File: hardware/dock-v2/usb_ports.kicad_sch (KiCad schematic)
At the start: 33 parts, among them J201 TYPE-C-31-M-12, J202 TYPE-C-31-M-12, J203 TYPE-C-31-M-12, U201 TPD4E1U06DBVR, U202 SY6280AAC, U203 TPD4E1U06DBVR, U204 TPD4E1U06DBVR

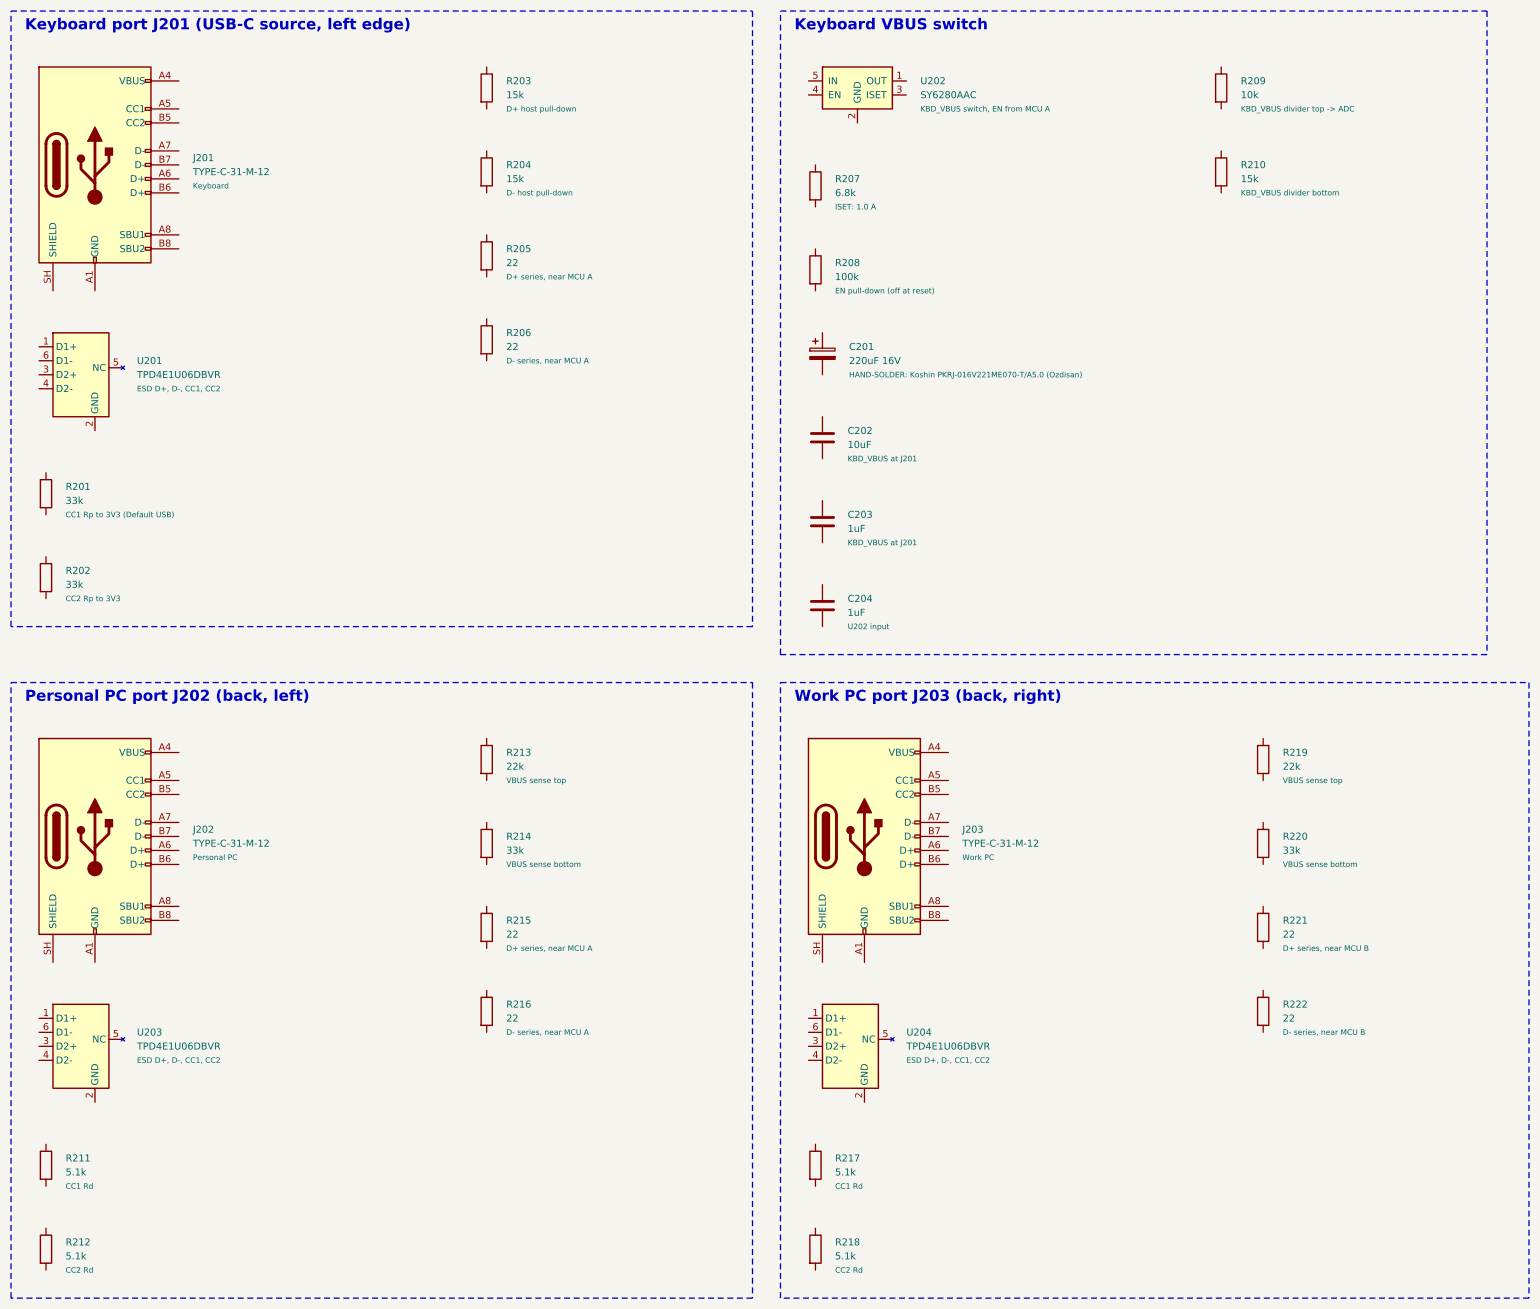
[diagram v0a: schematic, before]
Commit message: Dock v2 schematic: wiring in progress (user's work, snapshot before fixes)
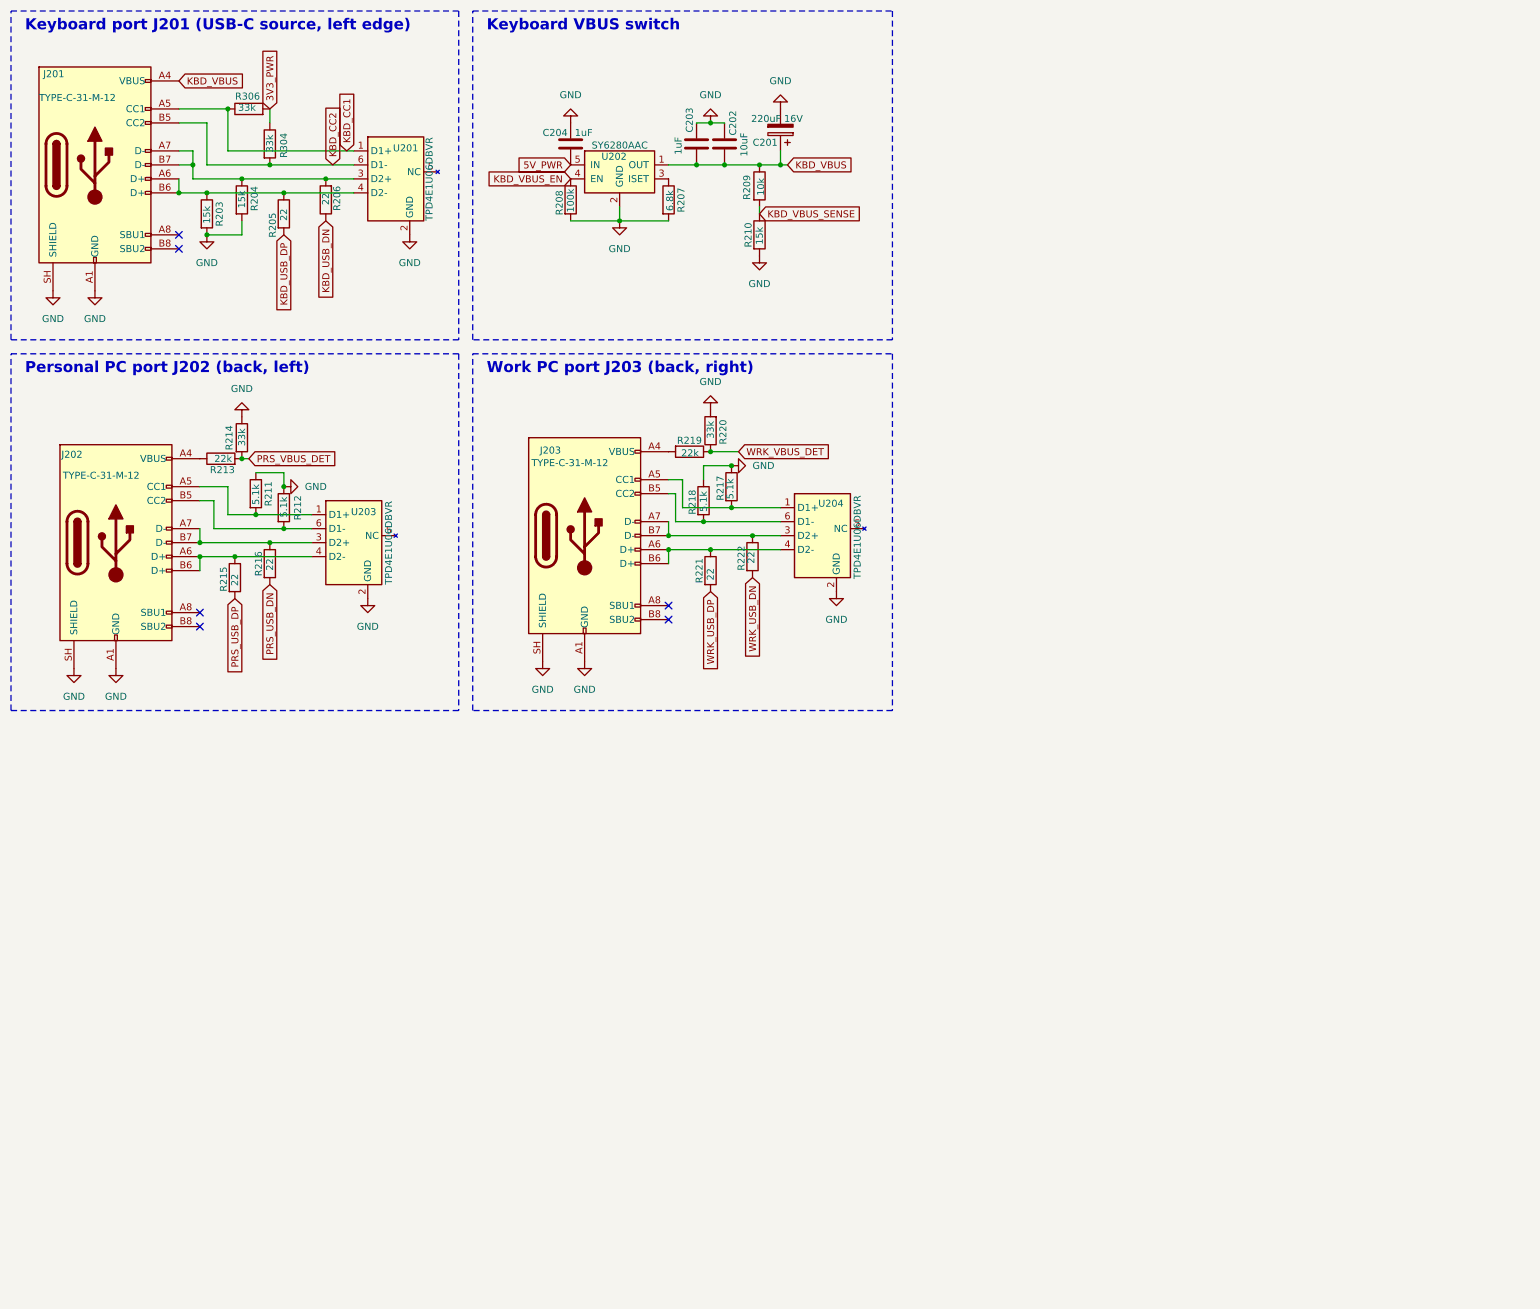
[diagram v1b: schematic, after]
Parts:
- removed R201, R202: 33k, Resistor_SMD:R_0402_1005Metric, symbol Device:R
- added R304, R306: 33k, Resistor_SMD:R_0402_1005Metric, symbol Device:R
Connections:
- net WRK_VBUS_DET: now reaches R219.1
- net WRK_VBUS_DET: now also R220.1
- net at R219.2: now also J203.A4 (VBUS), J203.A9 (VBUS), J203.B4 (VBUS), J203.B9 (VBUS)
- net GND: now reaches R217.1
- net GND: now also C201.2, C202.1, C203.2, C204.1, J201.A1 (GND), J201.A12 (GND), J201.B1 (GND), J201.B12 (GND), J201.SH (SHIELD), J202.A1 (GND), J202.A12 (GND), J202.B1 (GND), J202.B12 (GND), J202.SH (SHIELD), J203.A1 (GND), J203.A12 (GND), J203.B1 (GND), J203.B12 (GND), J203.SH (SHIELD), R203.2, R204.2, R207.2, R208.2, R210.2, R211.1, R212.1, R214.1, R218.1, R220.2, U201.2 (GND), U202.2 (GND), U203.2 (GND), U204.2 (GND)
- net at R217.2: now also J203.A5 (CC1), U204.1 (D1+)
- net PRS_VBUS_DET: now reaches R214.2
- net PRS_VBUS_DET: now also R213.2
- net KBD_VBUS: now reaches C201.1
- net KBD_VBUS: now also C202.2, C203.1, J201.A4 (VBUS), J201.A9 (VBUS), J201.B4 (VBUS), J201.B9 (VBUS), R209.1, U202.1 (OUT)
- net at U203.1 (D1+): now also J202.A5 (CC1), R211.2
- net at U203.3 (D2+): now also J202.A7 (D-), J202.B7 (D-), R216.1
- net at U203.4 (D2-): now also J202.A6 (D+), J202.B6 (D+), R215.1
- net at U203.6 (D1-): now also J202.B5 (CC2), R212.2
- net KBD_VBUS_EN: now reaches R208.1
- net KBD_VBUS_EN: now also U202.4 (EN)
- net KBD_VBUS_SENSE: now reaches R209.2
- net KBD_VBUS_SENSE: now also R210.1
- net KBD_CC1: now reaches J201.A5 (CC1)
- net KBD_CC1: now also U201.1 (D1+), R306.1
- net at J201.A6 (D+): now also J201.B6 (D+), R203.1, R205.1, U201.4 (D2-)
- net at J201.A7 (D-): now also J201.B7 (D-), R204.1, R206.2, U201.3 (D2+)
- net KBD_CC2: now reaches J201.B5 (CC2)
- net KBD_CC2: now also U201.6 (D1-), R304.2
- net at R207.1: now also U202.3 (ISET)
- net at J202.A4 (VBUS), J202.A9 (VBUS), J202.B4 (VBUS)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: now also R213.1
- net at U204.3 (D2+): now also J203.A7 (D-), J203.B7 (D-), R222.1
- net at U204.4 (D2-): now also J203.A6 (D+), J203.B6 (D+), R221.1
- net at U204.6 (D1-): now also J203.B5 (CC2), R218.2
- net PRS_USB_DP: now reaches R215.2
- net KBD_USB_DP: now reaches R205.2
- net KBD_USB_DN: now reaches R206.1
- net WRK_USB_DP: now reaches R221.2
- net 5V_PWR: now reaches C204.2
- net 5V_PWR: now also U202.5 (IN)
- net WRK_USB_DN: now reaches R222.2
- net PRS_USB_DN: now reaches R216.2
- new net 3V3_PWR: R304.1, R306.2
- no-connect marks 0 -> 6
